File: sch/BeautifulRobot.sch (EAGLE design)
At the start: 9 parts, among them IC1 STC12C4052AD, Q1 12MHz

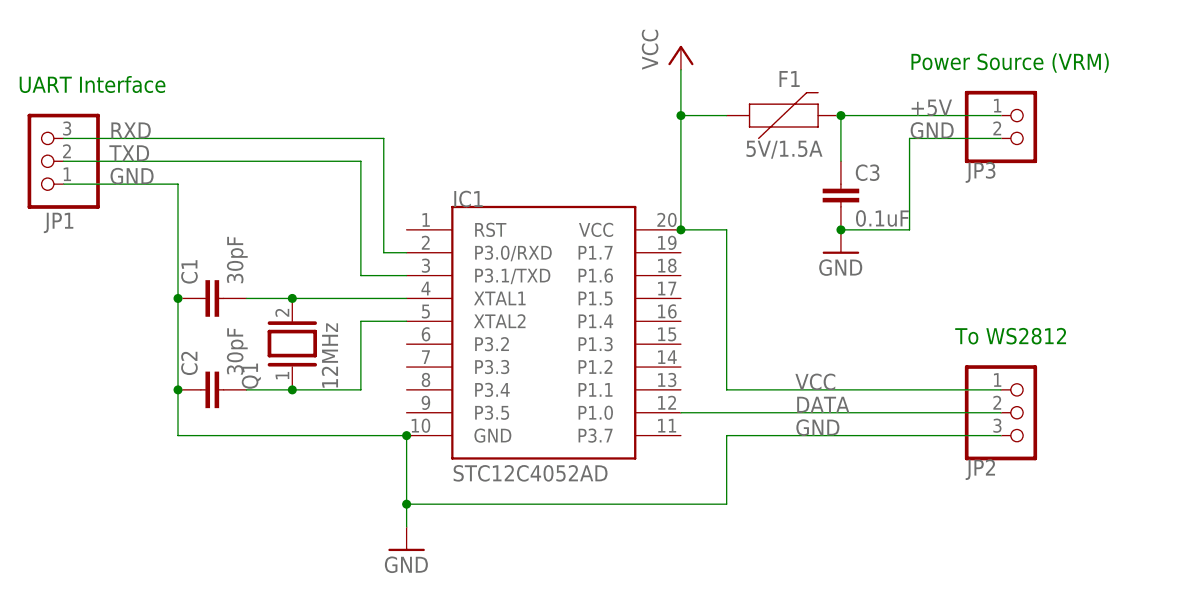
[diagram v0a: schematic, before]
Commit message: Schematic revision 2
Move resettable fuse to only affect the WS2812B.
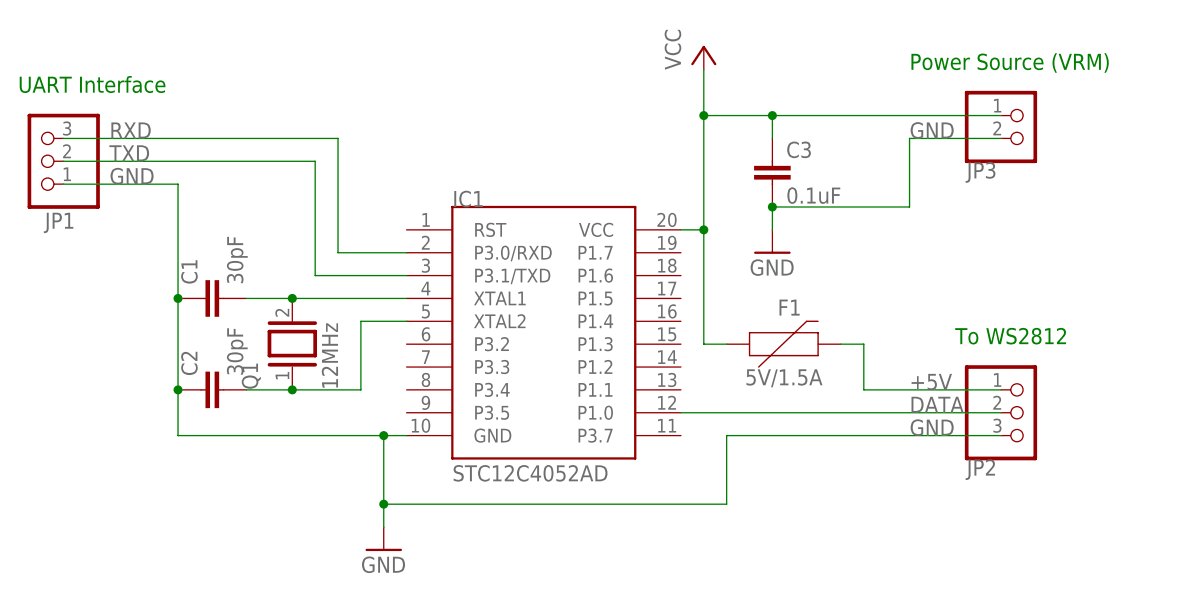
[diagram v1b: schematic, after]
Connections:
- net +5V: now also JP2.1; no longer C3.1, JP3.1
- net VCC: now also C3.1, JP3.1; no longer JP2.1
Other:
- moved on the sheet: C3, F1
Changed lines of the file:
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@@
 <attribute name="VALUE" x="119.38" y="73.66" size="1.778" layer="96"/>
 </instance>
-<instance part="P+1" gate="VCC" x="144.78" y="121.92" smashed="yes">
-<attribute name="VALUE" x="142.24" y="119.38" size="1.778" layer="96" rot="R90"/>
+<instance part="P+1" gate="VCC" x="147.32" y="121.92" smashed="yes">
+<attribute name="VALUE" x="144.78" y="119.38" size="1.778" layer="96" rot="R90"/>
 </instance>
-<instance part="GND1" gate="1" x="114.3" y="66.04" smashed="yes">
-<attribute name="VALUE" x="111.76" y="63.5" size="1.778" layer="96"/>
+<instance part="GND1" gate="1" x="111.76" y="66.04" smashed="yes">
+<attribute name="VALUE" x="109.22" y="63.5" size="1.778" layer="96"/>
 </instance>
 <instance part="Q1" gate="G$1" x="101.6" y="88.9" smashed="yes" rot="R90">
@@
 <attribute name="VALUE" x="176.53" y="106.68" size="1.778" layer="96"/>
 </instance>
-<instance part="F1" gate="G$1" x="154.94" y="114.3" smashed="yes">
-<attribute name="NAME" x="156.845" y="117.475" size="1.778" layer="95" font="vector" align="bottom-center"/>
-<attribute name="VALUE" x="156.21" y="111.506" size="1.778" layer="96" font="vector" align="top-center"/>
+<instance part="F1" gate="G$1" x="154.94" y="88.9" smashed="yes">
+<attribute name="NAME" x="156.845" y="92.075" size="1.778" layer="95" font="vector" align="bottom-center"/>
+<attribute name="VALUE" x="156.21" y="86.106" size="1.778" layer="96" font="vector" align="top-center"/>
 </instance>
-<instance part="GND2" gate="1" x="162.56" y="99.06" smashed="yes">
-<attribute name="VALUE" x="160.02" y="96.52" size="1.778" layer="96"/>
+<instance part="GND2" gate="1" x="154.94" y="99.06" smashed="yes">
+<attribute name="VALUE" x="152.4" y="96.52" size="1.778" layer="96"/>
 </instance>
-<instance part="C3" gate="G$1" x="162.56" y="106.68" smashed="yes">
-<attribute name="NAME" x="164.084" y="107.061" size="1.778" layer="95"/>
-<attribute name="VALUE" x="164.084" y="101.981" size="1.778" layer="96"/>
+<instance part="C3" gate="G$1" x="154.94" y="109.22" smashed="yes">
+<attribute name="NAME" x="156.464" y="109.601" size="1.778" layer="95"/>
+<attribute name="VALUE" x="156.464" y="104.521" size="1.778" layer="96"/>
 </instance>
 </instances>
@@
 <net name="GND" class="0">
 <segment>
-<pinref part="IC1" gate="G$1" pin="GND"/>
 <pinref part="GND1" gate="1" pin="GND"/>
-<wire x1="114.3" y1="68.58" x2="114.3" y2="71.12" width="0.1524" layer="91"/>
-<wire x1="114.3" y1="71.12" x2="114.3" y2="78.74" width="0.1524" layer="91"/>
-<wire x1="114.3" y1="78.74" x2="88.9" y2="78.74" width="0.1524" layer="91"/>
-<junction x="114.3" y="78.74"/>
-<pinref part="C1" gate="G$1" pin="1"/>
-<pinref part="C2" gate="G$1" pin="1"/>
-<wire x1="88.9" y1="93.98" x2="88.9" y2="83.82" width="0.1524" layer="91"/>
-<wire x1="88.9" y1="83.82" x2="88.9" y2="78.74" width="0.1524" layer="91"/>
-<junction x="88.9" y="83.82"/>
+<wire x1="111.76" y1="68.58" x2="111.76" y2="71.12" width="0.1524" layer="91"/>
 <pinref part="JP2" gate="A" pin="3"/>
 <wire x1="180.34" y1="78.74" x2="149.86" y2="78.74" width="0.1524" layer="91"/>
 <wire x1="149.86" y1="78.74" x2="149.86" y2="71.12" width="0.1524" layer="91"/>
-<wire x1="149.86" y1="71.12" x2="114.3" y2="71.12" width="0.1524" layer="91"/>
-<junction x="114.3" y="71.12"/>
-<label x="157.48" y="78.74" size="1.778" layer="95"/>
+<wire x1="149.86" y1="71.12" x2="111.76" y2="71.12" width="0.1524" layer="91"/>
+<label x="170.18" y="78.74" size="1.778" layer="95"/>
+<pinref part="IC1" gate="G$1" pin="GND"/>
+<wire x1="114.3" y1="78.74" x2="111.76" y2="78.74" width="0.1524" layer="91"/>
+<pinref part="C2" gate="G$1" pin="1"/>
+<pinref part="JP1" gate="A" pin="1"/>
+<wire x1="111.76" y1="78.74" x2="88.9" y2="78.74" width="0.1524" layer="91"/>
+<wire x1="88.9" y1="106.68" x2="76.2" y2="106.68" width="0.1524" layer="91"/>
+<pinref part="C1" gate="G$1" pin="1"/>
 <junction x="88.9" y="93.98"/>
 <wire x1="88.9" y1="93.98" x2="88.9" y2="106.68" width="0.1524" layer="91"/>
-<pinref part="JP1" gate="A" pin="1"/>
-<wire x1="88.9" y1="106.68" x2="76.2" y2="106.68" width="0.1524" layer="91"/>
+<wire x1="88.9" y1="93.98" x2="88.9" y2="83.82" width="0.1524" layer="91"/>
+<junction x="88.9" y="83.82"/>
+<wire x1="88.9" y1="83.82" x2="88.9" y2="78.74" width="0.1524" layer="91"/>
 <label x="81.28" y="106.68" size="1.778" layer="95"/>
+<wire x1="111.76" y1="71.12" x2="111.76" y2="78.74" width="0.1524" layer="91"/>
+<junction x="111.76" y="71.12"/>
+<junction x="111.76" y="78.74"/>
 </segment>
 <segment>
@@
 <pinref part="JP3" gate="G$1" pin="2"/>
 <wire x1="180.34" y1="111.76" x2="170.18" y2="111.76" width="0.1524" layer="91"/>
-<wire x1="170.18" y1="111.76" x2="170.18" y2="101.6" width="0.1524" layer="91"/>
+<wire x1="170.18" y1="111.76" x2="170.18" y2="104.14" width="0.1524" layer="91"/>
 <label x="170.18" y="111.76" size="1.778" layer="95"/>
-<wire x1="170.18" y1="101.6" x2="162.56" y2="101.6" width="0.1524" layer="91"/>
-<junction x="162.56" y="101.6"/>
+<wire x1="170.18" y1="104.14" x2="154.94" y2="104.14" width="0.1524" layer="91"/>
+<junction x="154.94" y="104.14"/>
+<wire x1="154.94" y1="104.14" x2="154.94" y2="101.6" width="0.1524" layer="91"/>
 </segment>
 </net>
 <net name="VCC" class="0">
 <segment>
+<pinref part="P+1" gate="VCC" pin="VCC"/>
+<wire x1="147.32" y1="114.3" x2="147.32" y2="119.38" width="0.1524" layer="91"/>
+<pinref part="JP3" gate="G$1" pin="1"/>
+<wire x1="180.34" y1="114.3" x2="154.94" y2="114.3" width="0.1524" layer="91"/>
+<pinref part="C3" gate="G$1" pin="1"/>
+<wire x1="154.94" y1="114.3" x2="147.32" y2="114.3" width="0.1524" layer="91"/>
+<wire x1="154.94" y1="111.76" x2="154.94" y2="114.3" width="0.1524" layer="91"/>
+<junction x="154.94" y="114.3"/>
 <pinref part="IC1" gate="G$1" pin="VCC"/>
-<pinref part="P+1" gate="VCC" pin="VCC"/>
-<wire x1="144.78" y1="101.6" x2="144.78" y2="114.3" width="0.1524" layer="91"/>
-<pinref part="JP2" gate="A" pin="1"/>
-<wire x1="144.78" y1="114.3" x2="144.78" y2="119.38" width="0.1524" layer="91"/>
-<wire x1="180.34" y1="83.82" x2="149.86" y2="83.82" width="0.1524" layer="91"/>
-<wire x1="149.86" y1="83.82" x2="149.86" y2="101.6" width="0.1524" layer="91"/>
-<wire x1="149.86" y1="101.6" x2="144.78" y2="101.6" width="0.1524" layer="91"/>
-<junction x="144.78" y="101.6"/>
-<label x="157.48" y="83.82" size="1.778" layer="95"/>
-<junction x="144.78" y="114.3"/>
+<wire x1="147.32" y1="101.6" x2="144.78" y2="101.6" width="0.1524" layer="91"/>
+<wire x1="147.32" y1="114.3" x2="147.32" y2="101.6" width="0.1524" layer="91"/>
+<junction x="147.32" y="114.3"/>
 <pinref part="F1" gate="G$1" pin="1"/>
-<wire x1="149.86" y1="114.3" x2="144.78" y2="114.3" width="0.1524" layer="91"/>
+<wire x1="147.32" y1="101.6" x2="147.32" y2="88.9" width="0.1524" layer="91"/>
+<wire x1="147.32" y1="88.9" x2="149.86" y2="88.9" width="0.1524" layer="91"/>
+<junction x="147.32" y="101.6"/>
 </segment>
 </net>
@@
 <segment>
 <pinref part="JP1" gate="A" pin="2"/>
-<wire x1="76.2" y1="109.22" x2="109.22" y2="109.22" width="0.1524" layer="91"/>
-<wire x1="109.22" y1="109.22" x2="109.22" y2="96.52" width="0.1524" layer="91"/>
+<wire x1="76.2" y1="109.22" x2="104.14" y2="109.22" width="0.1524" layer="91"/>
+<wire x1="104.14" y1="109.22" x2="104.14" y2="96.52" width="0.1524" layer="91"/>
 <pinref part="IC1" gate="G$1" pin="P3.1/TXD"/>
-<wire x1="109.22" y1="96.52" x2="114.3" y2="96.52" width="0.1524" layer="91"/>
+<wire x1="104.14" y1="96.52" x2="114.3" y2="96.52" width="0.1524" layer="91"/>
 <label x="81.28" y="109.22" size="1.778" layer="95"/>
 </segment>
@@
 <segment>
 <pinref part="JP1" gate="A" pin="3"/>
-<wire x1="76.2" y1="111.76" x2="111.76" y2="111.76" width="0.1524" layer="91"/>
-<wire x1="111.76" y1="111.76" x2="111.76" y2="99.06" width="0.1524" layer="91"/>
+<wire x1="76.2" y1="111.76" x2="106.68" y2="111.76" width="0.1524" layer="91"/>
+<wire x1="106.68" y1="111.76" x2="106.68" y2="99.06" width="0.1524" layer="91"/>
 <pinref part="IC1" gate="G$1" pin="P3.0/RXD"/>
-<wire x1="111.76" y1="99.06" x2="114.3" y2="99.06" width="0.1524" layer="91"/>
+<wire x1="106.68" y1="99.06" x2="114.3" y2="99.06" width="0.1524" layer="91"/>
 <label x="81.28" y="111.76" size="1.778" layer="95"/>
 </segment>
@@
 <pinref part="IC1" gate="G$1" pin="P1.0"/>
 <wire x1="180.34" y1="81.28" x2="144.78" y2="81.28" width="0.1524" layer="91"/>
-<label x="157.48" y="81.28" size="1.778" layer="95"/>
+<label x="170.18" y="81.28" size="1.778" layer="95"/>
 </segment>
 </net>
 <net name="+5V" class="0">
 <segment>
-<pinref part="JP3" gate="G$1" pin="1"/>
 <pinref part="F1" gate="G$1" pin="2"/>
-<wire x1="180.34" y1="114.3" x2="162.56" y2="114.3" width="0.1524" layer="91"/>
-<label x="170.18" y="114.3" size="1.778" layer="95"/>
-<pinref part="C3" gate="G$1" pin="1"/>
-<wire x1="162.56" y1="109.22" x2="162.56" y2="114.3" width="0.1524" layer="91"/>
-<junction x="162.56" y="114.3"/>
+<wire x1="162.56" y1="88.9" x2="165.1" y2="88.9" width="0.1524" layer="91"/>
+<wire x1="165.1" y1="88.9" x2="165.1" y2="83.82" width="0.1524" layer="91"/>
+<pinref part="JP2" gate="A" pin="1"/>
+<wire x1="165.1" y1="83.82" x2="180.34" y2="83.82" width="0.1524" layer="91"/>
+<label x="170.18" y="83.82" size="1.778" layer="95"/>
 </segment>
 </net>

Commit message: Move fuse in schematic to include the whole circuit
The resettable fuse was moved so that now it lies before the whole
circuit rather than just the LED strip. This means that in case of
overcurrent, the MCU will lose power and be reset, which will cause it
to start back up with all the LEDs off.
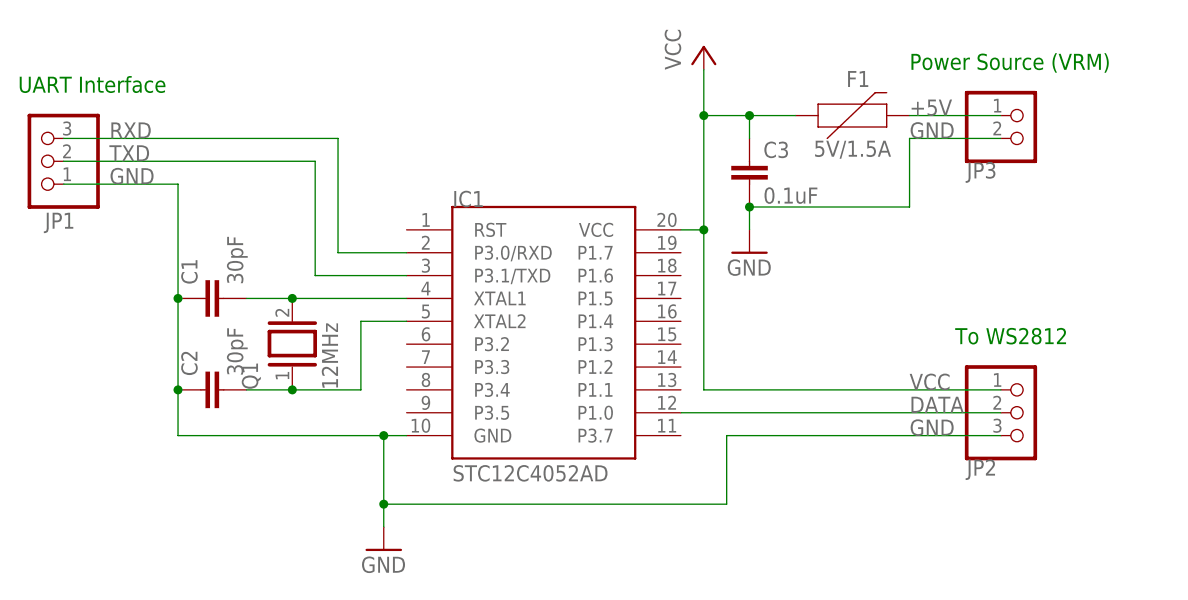
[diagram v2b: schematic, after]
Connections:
- net +5V: now also JP3.1; no longer JP2.1
- net VCC: now also JP2.1; no longer JP3.1
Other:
- moved on the sheet: C3, F1
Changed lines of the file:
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@@
 <attribute name="VALUE" x="176.53" y="106.68" size="1.778" layer="96"/>
 </instance>
-<instance part="F1" gate="G$1" x="154.94" y="88.9" smashed="yes">
-<attribute name="NAME" x="156.845" y="92.075" size="1.778" layer="95" font="vector" align="bottom-center"/>
-<attribute name="VALUE" x="156.21" y="86.106" size="1.778" layer="96" font="vector" align="top-center"/>
+<instance part="F1" gate="G$1" x="162.56" y="114.3" smashed="yes">
+<attribute name="NAME" x="164.465" y="117.475" size="1.778" layer="95" font="vector" align="bottom-center"/>
+<attribute name="VALUE" x="163.83" y="111.506" size="1.778" layer="96" font="vector" align="top-center"/>
 </instance>
-<instance part="GND2" gate="1" x="154.94" y="99.06" smashed="yes">
-<attribute name="VALUE" x="152.4" y="96.52" size="1.778" layer="96"/>
+<instance part="GND2" gate="1" x="152.4" y="99.06" smashed="yes">
+<attribute name="VALUE" x="149.86" y="96.52" size="1.778" layer="96"/>
 </instance>
-<instance part="C3" gate="G$1" x="154.94" y="109.22" smashed="yes">
-<attribute name="NAME" x="156.464" y="109.601" size="1.778" layer="95"/>
-<attribute name="VALUE" x="156.464" y="104.521" size="1.778" layer="96"/>
+<instance part="C3" gate="G$1" x="152.4" y="109.22" smashed="yes">
+<attribute name="NAME" x="153.924" y="109.601" size="1.778" layer="95"/>
+<attribute name="VALUE" x="153.924" y="104.521" size="1.778" layer="96"/>
 </instance>
 </instances>
@@
 <wire x1="170.18" y1="111.76" x2="170.18" y2="104.14" width="0.1524" layer="91"/>
 <label x="170.18" y="111.76" size="1.778" layer="95"/>
-<wire x1="170.18" y1="104.14" x2="154.94" y2="104.14" width="0.1524" layer="91"/>
-<junction x="154.94" y="104.14"/>
-<wire x1="154.94" y1="104.14" x2="154.94" y2="101.6" width="0.1524" layer="91"/>
+<wire x1="170.18" y1="104.14" x2="152.4" y2="104.14" width="0.1524" layer="91"/>
+<junction x="152.4" y="104.14"/>
+<wire x1="152.4" y1="104.14" x2="152.4" y2="101.6" width="0.1524" layer="91"/>
 </segment>
 </net>
@@
 <pinref part="P+1" gate="VCC" pin="VCC"/>
 <wire x1="147.32" y1="114.3" x2="147.32" y2="119.38" width="0.1524" layer="91"/>
-<pinref part="JP3" gate="G$1" pin="1"/>
-<wire x1="180.34" y1="114.3" x2="154.94" y2="114.3" width="0.1524" layer="91"/>
-<pinref part="C3" gate="G$1" pin="1"/>
-<wire x1="154.94" y1="114.3" x2="147.32" y2="114.3" width="0.1524" layer="91"/>
-<wire x1="154.94" y1="111.76" x2="154.94" y2="114.3" width="0.1524" layer="91"/>
-<junction x="154.94" y="114.3"/>
+<wire x1="157.48" y1="114.3" x2="152.4" y2="114.3" width="0.1524" layer="91"/>
 <pinref part="IC1" gate="G$1" pin="VCC"/>
+<wire x1="152.4" y1="114.3" x2="147.32" y2="114.3" width="0.1524" layer="91"/>
 <wire x1="147.32" y1="101.6" x2="144.78" y2="101.6" width="0.1524" layer="91"/>
 <wire x1="147.32" y1="114.3" x2="147.32" y2="101.6" width="0.1524" layer="91"/>
 <junction x="147.32" y="114.3"/>
 <pinref part="F1" gate="G$1" pin="1"/>
-<wire x1="147.32" y1="101.6" x2="147.32" y2="88.9" width="0.1524" layer="91"/>
-<wire x1="147.32" y1="88.9" x2="149.86" y2="88.9" width="0.1524" layer="91"/>
+<pinref part="C3" gate="G$1" pin="1"/>
+<wire x1="152.4" y1="111.76" x2="152.4" y2="114.3" width="0.1524" layer="91"/>
+<junction x="152.4" y="114.3"/>
+<pinref part="JP2" gate="A" pin="1"/>
+<label x="170.18" y="83.82" size="1.778" layer="95"/>
+<wire x1="180.34" y1="83.82" x2="147.32" y2="83.82" width="0.1524" layer="91"/>
+<wire x1="147.32" y1="83.82" x2="147.32" y2="101.6" width="0.1524" layer="91"/>
 <junction x="147.32" y="101.6"/>
 </segment>
@@
 <segment>
 <pinref part="F1" gate="G$1" pin="2"/>
-<wire x1="162.56" y1="88.9" x2="165.1" y2="88.9" width="0.1524" layer="91"/>
-<wire x1="165.1" y1="88.9" x2="165.1" y2="83.82" width="0.1524" layer="91"/>
-<pinref part="JP2" gate="A" pin="1"/>
-<wire x1="165.1" y1="83.82" x2="180.34" y2="83.82" width="0.1524" layer="91"/>
-<label x="170.18" y="83.82" size="1.778" layer="95"/>
+<pinref part="JP3" gate="G$1" pin="1"/>
+<wire x1="170.18" y1="114.3" x2="180.34" y2="114.3" width="0.1524" layer="91"/>
+<label x="170.18" y="114.3" size="1.778" layer="95"/>
 </segment>
 </net>

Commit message: Add missing resistor in schematic
Add missing 330R resistor in the data line of the WS2812B. README.md is
also updated.
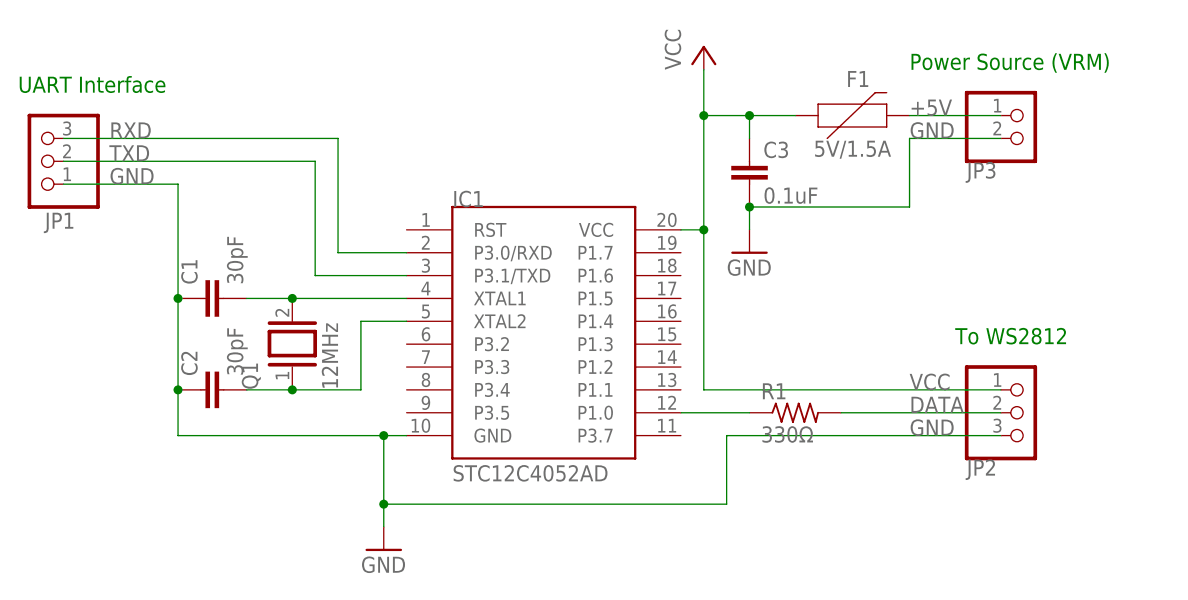
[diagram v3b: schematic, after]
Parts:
- added R1: 330Ω, rcl:R-US_0204/7
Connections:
- new net N$3: IC1.P1.0, R1.1
- net DATA: now also R1.2; no longer IC1.P1.0
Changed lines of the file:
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@@
 <part name="GND2" library="supply1" library_urn="urn:adsk.eagle:library:371" deviceset="GND" device=""/>
 <part name="C3" library="rcl" library_urn="urn:adsk.eagle:library:334" deviceset="C-EU" device="025-025X050" package3d_urn="urn:adsk.eagle:package:23629/2" value="0.1uF"/>
+<part name="R1" library="rcl" library_urn="urn:adsk.eagle:library:334" deviceset="R-US_" device="0204/7" package3d_urn="urn:adsk.eagle:package:23498/2" value="330Ω"/>
 </parts>
 <sheets>
@@
 <attribute name="NAME" x="153.924" y="109.601" size="1.778" layer="95"/>
 <attribute name="VALUE" x="153.924" y="104.521" size="1.778" layer="96"/>
+</instance>
+<instance part="R1" gate="G$1" x="157.48" y="81.28" smashed="yes">
+<attribute name="NAME" x="153.67" y="82.7786" size="1.778" layer="95"/>
+<attribute name="VALUE" x="153.67" y="77.978" size="1.778" layer="96"/>
 </instance>
 </instances>
@@
 <segment>
 <pinref part="JP2" gate="A" pin="2"/>
-<pinref part="IC1" gate="G$1" pin="P1.0"/>
-<wire x1="180.34" y1="81.28" x2="144.78" y2="81.28" width="0.1524" layer="91"/>
 <label x="170.18" y="81.28" size="1.778" layer="95"/>
+<wire x1="180.34" y1="81.28" x2="162.56" y2="81.28" width="0.1524" layer="91"/>
+<pinref part="R1" gate="G$1" pin="2"/>
 </segment>
 </net>
@@
 </segment>
 </net>
+<net name="N$3" class="0">
+<segment>
+<pinref part="IC1" gate="G$1" pin="P1.0"/>
+<wire x1="152.4" y1="81.28" x2="144.78" y2="81.28" width="0.1524" layer="91"/>
+<pinref part="R1" gate="G$1" pin="1"/>
+</segment>
+</net>
